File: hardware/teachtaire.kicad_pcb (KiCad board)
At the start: 4 copper layers, 60 x 60 mm, 50 parts, among them J1 Conn_Coaxial, J3 ESQ-110-X-X-D, J4 XT30PW-M, J5 Conn_01x10, J6 Conn_Coaxial, Q1 PMOS, Q2 NMOS, U1 MAX-M10S, U10 radio_thing, U2 STM32F072C8Tx, U3 TJA1051T/3/1J, U4 TLV70433DBVT, U5 LT6003HDC-TRMPBF, U6 NC7WZ07P6X, U7 NC7WZ07P6X

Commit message: minorest of changes
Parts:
- removed U10: radio_thing, radio_breakout:radio_breakout
- added G***: LOGO, LOGO, F.Cu at (180.0, 98.5)
- added G***: LOGO, LOGO, F.Cu at (171.0, 111.5)
- added G***: LOGO, LOGO, F.Cu at (154.0, 81.0)
- added U8: RF-LORA-868-SO, footprints:XCVR_RF-LORA-868-SO, F.Cu at (146.0, 95.2)
- moved U5 22.9 mm to (179.4, 88.1), turned to 0 degrees
- moved J6 19.9 mm to (153.6, 73.3)
- moved D1 16.9 mm to (165.7, 101.0), turned to 180 degrees
- moved C28 15.8 mm to (167.6, 113.9), turned to -90 degrees
- moved R1 15.2 mm to (163.8, 101.0), turned to 0 degrees
- moved C30 14.3 mm to (166.6, 113.9), turned to -90 degrees
- moved C31 13.8 mm to (155.2, 112.7), turned to 180 degrees
- moved C2 12.0 mm to (176.0, 91.4)
- moved R3 11.1 mm to (171.6, 88.7), turned to -90 degrees
- moved Q2 10.4 mm to (172.2, 92.5)
- moved J1 10.2 mm to (175.5, 96.7), turned to 180 degrees
- moved Q1 9.99 mm to (174.1, 89.2)
- moved C39 9.76 mm to (163.7, 86.3), turned to 0 degrees
- moved C1 9.40 mm to (175.0, 93.6), turned to 180 degrees
- moved U4 9.24 mm to (160.5, 86.0), turned to 180 degrees
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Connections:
- Q1 pad 1: +3.3V -> /GNSS_Bias_T/Antenna Supply
- R3 pad 1: +3.3V -> /GNSS_Bias_T/Antenna Supply
- U1 pad 14: unconnected-(U1-VCC_RF-Pad14) -> /GNSS_Bias_T/Antenna Supply
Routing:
- net GND: track 89.7 -> 8.82 mm, vias 34 -> 120
- net 5VLOGIC: track 62.4 -> 30.7 mm, vias 5 -> 1
- net Net-(J6-In): track 45.4 -> 14.5 mm
- net Net-(U5--IN): track 40.0 -> 12.1 mm, vias 2 -> 0
- net Net-(U5-+IN): track 27.2 -> 3.06 mm, vias 2 -> 0
- net LoRa_NSS: track 36.5 -> 17.4 mm
- net /GNSS_Bias_T/Antenna Supply: track 0.00 -> 16.3 mm, vias 0 -> 2
- net /GNSS_Bias_T/ANT_OFF_N: track 18.9 -> 4.18 mm, vias 2 -> 0
- net LoRa_MOSI: track 33.6 -> 19.1 mm
- net /GNSS_Bias_T/V_ANT: track 21.4 -> 8.03 mm, vias 2 -> 0
- net Net-(J1-In): track 15.8 -> 2.46 mm, vias 2 -> 0
- net SWCLK1: track 56.7 -> 44.5 mm, vias 4 -> 1
- net LoRa_MISO: track 33.4 -> 21.4 mm
- net Net-(Q1-S): track 11.4 -> 2.23 mm
- net Net-(U1-TIMEPULSE): track 2.13 -> 10.1 mm
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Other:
- board text added: "Teachtaire V1.0"

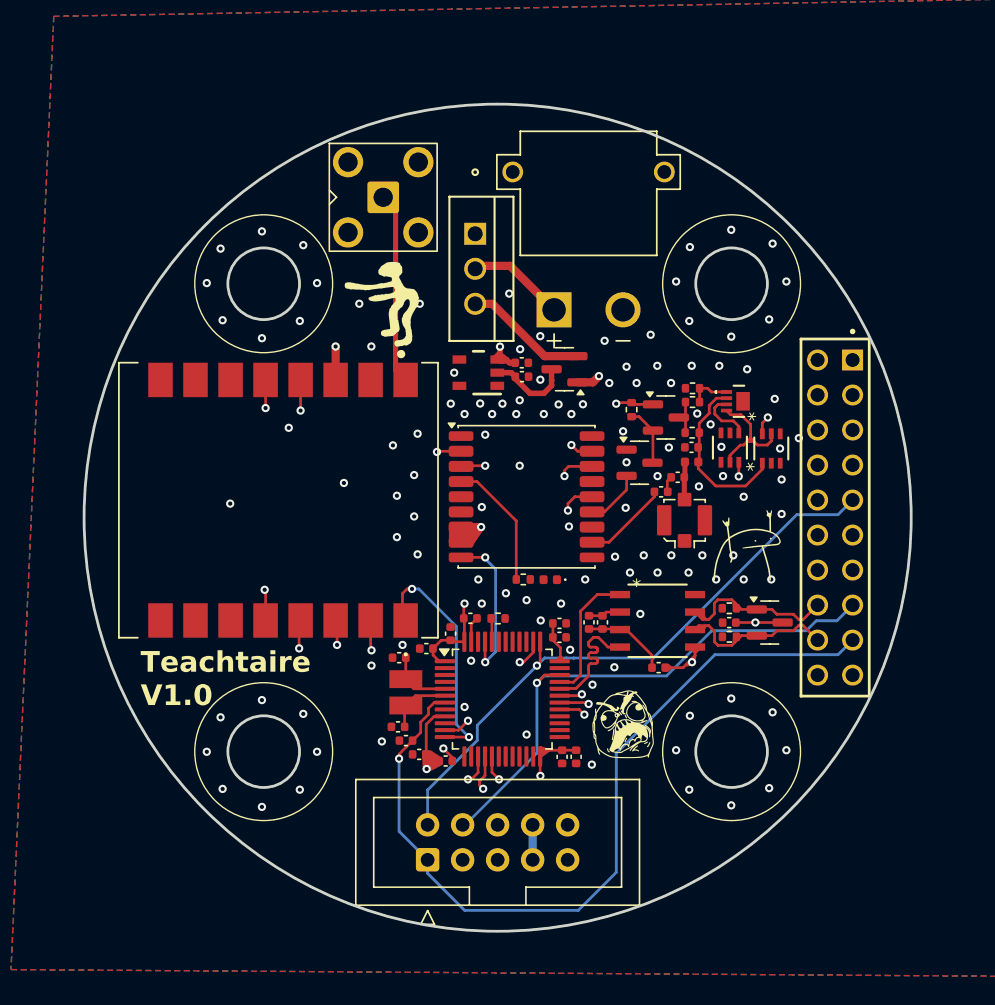
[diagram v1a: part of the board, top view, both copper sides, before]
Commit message: Changes from Reddit review 1
Changed connector, impedance matched the RF traces, changed board to square
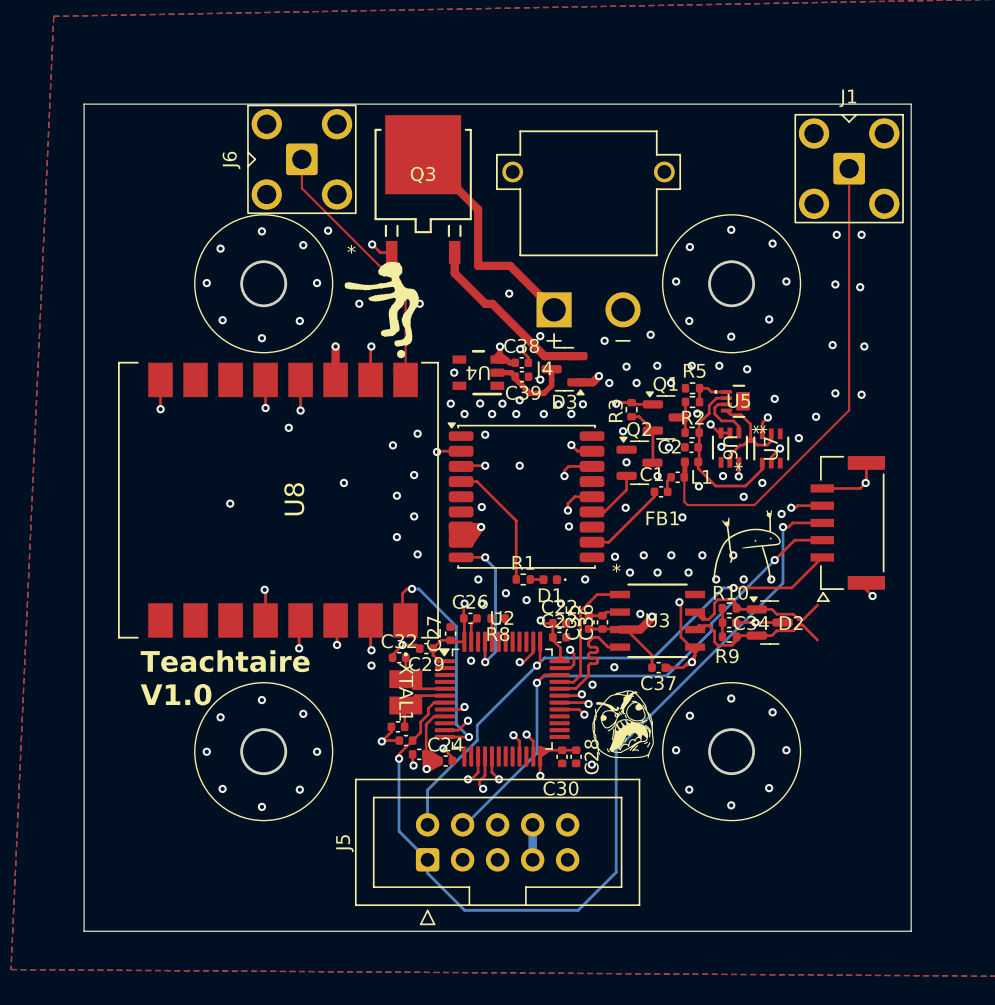
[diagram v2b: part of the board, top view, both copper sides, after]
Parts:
- removed J3: ESQ-110-X-X-D, footprints:SAMTEC_ESQ-110-14-G-D
- removed MOSFET1: IPP80P03P4L04AKSA1, footprints:IPP80P03P4L04AKSA1
- added J2: 5023860570, footprints:MOLEX_5023860570, F.Cu at (187.4, 96.9)
- added Q3: IPD90P04P4L04ATMA1, footprints:PG-TO252-3-313_INF-L, F.Cu at (156.5, 71.6)
- J1: footprint Connector_Coaxial:U.FL_Molex_MCRF_73412-0110_Vertical -> Connector_Coaxial:SMA_BAT_Wireless_BWSMA-KWE-Z001
- moved J1 28.2 mm to (187.4, 71.2), turned to -90 degrees
- moved J6 6.51 mm to (147.7, 70.5)
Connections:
- U2 pad 21: unconnected-(U2-PB10-Pad21) -> LoRa_DIO2
- U8 pad 8: unconnected-(U8-DIO2-Pad8) -> LoRa_DIO2
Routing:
- net LoRa_DIO2: track 0.00 -> 39.6 mm, vias 0 -> 2
- net Net-(J1-In): track 2.46 -> 35.2 mm
- net GND: track 8.82 -> 34.8 mm, vias 120 -> 135
- net 5VLOGIC: track 30.7 -> 55.1 mm, vias 1 -> 2
- net +3.3V: track 128.3 -> 147.2 mm, vias 8 -> 10
- net Net-(Q3-D): track 7.13 -> 16.5 mm
- net Net-(J6-In): track 14.5 -> 20.7 mm
- net SWCLK1: track 44.5 -> 40.6 mm, vias 1 -> 2
- net Net-(Q3-S): track 8.99 -> 12.9 mm
- net NRST: track 60.2 -> 64.0 mm, vias 1 -> 2
- net 5VSERVO: track 2.54 -> 0.00 mm
- net Net-(C34-Pad1): track 0.00 -> 2.08 mm
- net Net-(D1-A): track 0.00 -> 0.97 mm
- net SWDIO: vias 1 -> 2
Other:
- outline, holes or cut-outs redrawn

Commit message: lots to be sorted
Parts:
- removed J5: Conn_01x10, Connector_IDC:IDC-Header_2x05_P2.54mm_Vertical
- added G***: LOGO, LOGO, F.Cu at (140.3, 122.8)
- added J3: ESQ-110-X-X-D, footprints:SAMTEC_ESQ-110-14-G-D, F.Cu at (187.6, 96.3)
- moved J2 35.5 mm to (162.2, 122.0), turned to 180 degrees
- moved G*** 2.00 mm to (156.0, 81.0)
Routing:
- added copper zone on In3.Cu, net GND
- added copper zone on In4.Cu, net GND
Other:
- copper layers 4 -> 6
- board text added: "SWCLK SWDIO NRST 3v3 GND"
- board text added: "teachtaire-v1.0"
- board text removed: "Teachtaire V1.0"

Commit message: many fatal fuck-ups found
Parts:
- removed C38: 1uF, Capacitor_SMD:C_0402_1005Metric
- removed C39: 100nF, Capacitor_SMD:C_0402_1005Metric
- removed FB1: FerriteBead, Capacitor_SMD:C_0402_1005Metric
- added C10: 0.1uf, Capacitor_SMD:C_0402_1005Metric, F.Cu at (208.2, 116.1)
- added C11: 4.7uF, Capacitor_SMD:C_0402_1005Metric, F.Cu at (97.9, 71.0)
- added C12: 100nF, Capacitor_SMD:C_0402_1005Metric, F.Cu at (97.9, 72.9)
- added C13: 4.7uF, Capacitor_SMD:C_0402_1005Metric, F.Cu at (97.9, 74.9)
- added C14: 100nF, Capacitor_SMD:C_0402_1005Metric, F.Cu at (97.9, 76.9)
- added C3: 39pf, Capacitor_SMD:C_0402_1005Metric, F.Cu at (205.4, 110.2)
- added C4: 0.1uf, Capacitor_SMD:C_0402_1005Metric, F.Cu at (205.4, 112.2)
- added C47: 22uf, Capacitor_SMD:C_0402_1005Metric, F.Cu at (211.1, 110.2)
- added C48: 22uf, Capacitor_SMD:C_0402_1005Metric, F.Cu at (211.1, 112.2)
- added C5: 22uf, Capacitor_SMD:C_0402_1005Metric, F.Cu at (205.4, 114.2)
- added C50: 1uf, Capacitor_SMD:C_0402_1005Metric, F.Cu at (211.1, 114.2)
- added C51: 1uf, Capacitor_SMD:C_0402_1005Metric, F.Cu at (211.1, 116.1)
- added C6: 22uf, Capacitor_SMD:C_0402_1005Metric, F.Cu at (205.4, 116.1)
- added C7: 1uf, Capacitor_SMD:C_0402_1005Metric, F.Cu at (208.2, 110.2)
- added C8: 22uf, Capacitor_SMD:C_0402_1005Metric, F.Cu at (208.2, 112.2)
- added C9: 22uf, Capacitor_SMD:C_0402_1005Metric, F.Cu at (208.2, 114.2)
- added GND1: TestPoint, TestPoint:TestPoint_Pad_D2.0mm, F.Cu at (94.5, 72.0)
- added Q4: NMOS, Package_TO_SOT_SMD:SOT-23, F.Cu at (101.8, 72.2)
- added R11: 10kΩ, Resistor_SMD:R_0402_1005Metric, F.Cu at (100.8, 75.4)
- added R12: 100kΩ, Resistor_SMD:R_0402_1005Metric, F.Cu at (214.0, 114.2)
- added R14: 0Ω, Resistor_SMD:R_0402_1005Metric, F.Cu at (93.9, 81.1)
- added R15: 0Ω, Resistor_SMD:R_0402_1005Metric, F.Cu at (93.9, 83.1)
- added R6: 10kΩ, Resistor_SMD:R_0402_1005Metric, F.Cu at (214.0, 110.2)
- added R7: 53.6kΩ, Resistor_SMD:R_0402_1005Metric, F.Cu at (214.0, 112.2)
- added U9: TLV75533PDRV, Package_SON:WSON-6-1EP_2x2mm_P0.65mm_EP1x1.6mm, F.Cu at (205.8, 119.0)
- added VBCKP1: TestPoint, TestPoint:TestPoint_Pad_D2.0mm, F.Cu at (94.5, 76.1)
- J4: value XT30PW-M -> 39-29-1048; footprint footprints:AMASS_XT30PW-M -> footprints:MOLEX_39-29-1048
- R10, R9: value 60 Ω -> 60Ω
- U4: value TLV70433DBVT -> MPM3650CGQW-P; footprint footprints:DBV0005A_N -> footprints:QFN-24_MPM3650_MNP
- moved J1 101.7 mm to (87.5, 52.0), turned to 0 degrees
- moved D1 99.6 mm to (71.2, 69.4), turned to 0 degrees
- moved R1 95.9 mm to (73.2, 69.5), turned to 180 degrees
- moved L1 95.4 mm to (87.1, 57.9), turned to 180 degrees
- moved U1 94.6 mm to (75.0, 63.0), turned to 90 degrees
- moved C1 94.4 mm to (88.0, 56.8), turned to 0 degrees
- moved Q1 80.3 mm to (98.9, 61.3)
- moved Q2 80.3 mm to (96.9, 64.6)
- moved R2 80.3 mm to (100.8, 62.4)
- moved R3 80.3 mm to (96.4, 60.7)
- moved R4 80.3 mm to (100.8, 60.2)
- moved R5 80.3 mm to (100.8, 59.2)
- moved U5 80.3 mm to (104.2, 60.1)
- moved C2 80.3 mm to (100.7, 63.5)
- moved U6 80.3 mm to (103.5, 63.5)
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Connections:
- net SWCLK1 renamed SWCLK
- C1 pad 2: Net-(C1-Pad2) -> /GNSS_Bias_T/RF_IN
- C22 pad 1: +3.3V -> +3V3D
- C23 pad 1: +3.3V -> +3V3D
- C24 pad 1: +3.3V -> +3V3D
- C25 pad 1: +3.3V -> +3V3D
- C26 pad 1: +3.3V -> +3V3D
- C27 pad 1: +3.3V -> +3V3D
- C28 pad 1: +3.3V -> +3V3D
- C29 pad 1: +3.3V -> +3V3D
- C30 pad 1: +3.3V -> +3V3D
- C37 pad 1: +3.3V -> 5VLOGIC
- C37 pad 2: 5VLOGIC -> +3V3D
- D1 pad 1: GND -> Net-(D1-K)
- Q1 pad 1: /GNSS_Bias_T/Antenna Supply -> Net-(Q1-D)
- Q1 pad 3: Net-(Q1-S) -> /GNSS_Bias_T/Antenna Supply
- Q2 pad 1: GND -> Net-(Q1-G)
- Q2 pad 3: Net-(Q1-G) -> GND
- R1 pad 1: Net-(U1-TIMEPULSE) -> +3.3V
- R2 pad 2: Net-(Q1-S) -> Net-(Q1-D)
- R4 pad 1: Net-(Q1-S) -> Net-(Q1-D)
- U1 pad 4: Net-(U1-TIMEPULSE) -> Net-(Q4-G)
- U1 pad 6: unconnected-(U1-V_BCKP-Pad6) -> Net-(U1-V_BCKP)
- U1 pad 7: +3.3V -> +3V3RF
- U1 pad 8: +3.3V -> +3V3RF
- U2 pad 1: +3.3V -> +3V3D
- U2 pad 24: +3.3V -> +3V3D
- U2 pad 36: +3.3V -> +3V3D
- U2 pad 48: +3.3V -> +3V3D
- U2 pad 9: +3.3V -> +3V3D
- U3 pad 5: +3.3V -> +3V3D
- U4 pad 2: VBAT -> GND
- U4 pad 3: +3.3V -> GND
- U5 pad 4: /GNSS_Bias_T/V_ANT -> +3V3D
- U6 pad 5: /GNSS_Bias_T/V_ANT -> +3V3D
- U6 pad 6: /GNSS_Bias_T/ANT_DETECT -> Net-(U6-Y1)
- U7 pad 5: /GNSS_Bias_T/V_ANT -> +3V3D
- U7 pad 6: /GNSS_Bias_T/ANT_SHORT_N -> Net-(U7-Y1)
- U8 pad 3: +3.3V -> +3V3RF
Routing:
- net NRST: track 64.0 -> 4.18 mm, vias 2 -> 0
- net +3.3V: track 147.2 -> 97.6 mm, vias 10 -> 0
- net 5VLOGIC: track 55.1 -> 9.41 mm, vias 2 -> 1
- net SWCLK: track 40.6 -> 0.00 mm, vias 2 -> 0
- net SWDIO: track 39.8 -> 0.00 mm, vias 2 -> 0
- net LoRa_DIO2: track 39.6 -> 1.72 mm, vias 2 -> 1
- net LoRa_RX_SWITCH: track 35.4 -> 1.95 mm, vias 2 -> 1
- net Net-(J1-In): track 35.2 -> 5.97 mm
- net LoRa_TX_SWITCH: track 30.6 -> 1.60 mm, vias 2 -> 1
- net LoRa_RESET: track 25.1 -> 1.96 mm, vias 2 -> 1
- net PA10: track 25.9 -> 3.20 mm
- net PA9: track 25.1 -> 3.69 mm
- net Net-(J6-In): track 20.7 -> 0.00 mm
- net LoRa_SCK: track 22.0 -> 1.42 mm, vias 2 -> 1
- net +3V3D: track 0.00 -> 20.5 mm, vias 0 -> 4
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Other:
- outline, holes or cut-outs redrawn
- board text added: "backup pwr"
- board text added: "teachtaire-v1.2"
- board text removed: "teachtaire-v1.0"

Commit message: fixed the fuck-ups
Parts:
- removed the C10 at (208.2, 116.1)
- removed the C3 at (205.4, 110.2)
- removed the C4 at (205.4, 112.2)
- removed the C5 at (205.4, 114.2)
- removed the C6 at (205.4, 116.1)
- removed the C7 at (208.2, 110.2)
- removed the C8 at (208.2, 112.2)
- removed the C9 at (208.2, 114.2)
- removed the R6 at (214.0, 110.2)
- removed the R7 at (214.0, 112.2)
- removed the U4 at (213.0, 121.1)
- added C23: 39pf, Capacitor_SMD:C_0402_1005Metric, F.Cu at (188.9, 70.8)
- added C24: 0.1uf, Capacitor_SMD:C_0402_1005Metric, F.Cu at (188.9, 72.8)
- added C25: 22uf, Capacitor_SMD:C_0402_1005Metric, F.Cu at (188.9, 74.7)
- added C26: 22uf, Capacitor_SMD:C_0402_1005Metric, F.Cu at (188.9, 76.7)
- added C28: 1uf, Capacitor_SMD:C_0402_1005Metric, F.Cu at (188.9, 78.7)
- added C30: 22uf, Capacitor_SMD:C_0402_1005Metric, F.Cu at (188.9, 80.7)
- added C31: 22uf, Capacitor_SMD:C_0402_1005Metric, F.Cu at (191.8, 70.8)
- added C32: 0.1uf, Capacitor_SMD:C_0402_1005Metric, F.Cu at (191.8, 72.8)
- added C34: 4.7uf, Capacitor_SMD:C_0402_1005Metric, F.Cu at (191.8, 74.7)
- added C35: 4.7uf, Capacitor_SMD:C_0402_1005Metric, F.Cu at (191.8, 76.7)
- added C37: 10uf, Capacitor_SMD:C_0402_1005Metric, F.Cu at (191.8, 78.7)
- added D4: BAT54J, Diode_SMD:D_SOD-323F, F.Cu at (135.7, 117.5)
- added R13: 53.6kΩ, Resistor_SMD:R_0402_1005Metric, F.Cu at (201.0, 72.8)
- added R14: 100kΩ, Resistor_SMD:R_0402_1005Metric, F.Cu at (201.0, 74.8)
- added R15: 33.2kΩ, Resistor_SMD:R_0402_1005Metric, F.Cu at (201.0, 76.8)
- added U8: MPM3650CGQW-P, footprints:QFN-24_MPM3650_MNP, F.Cu at (190.2, 86.3)
- added VR1: LT3045EDD_PBF, footprints:SON50P300X300X80-11N, F.Cu at (202.2, 85.6)
- R12: value 100kΩ -> 10kΩ
- moved J5 100.2 mm to (161.3, 119.8), turned to -90 degrees
- moved L1 91.7 mm to (155.1, 119.3), turned to 90 degrees
- moved C21 90.1 mm to (152.4, 119.8), turned to 180 degrees
- moved U1 88.5 mm to (145.5, 116.5), turned to 0 degrees
- moved R8 80.8 mm to (161.0, 114.0)
- moved R9 80.8 mm to (161.0, 113.0)
- moved U6 80.6 mm to (166.7, 113.4), turned to 90 degrees
- moved U5 79.6 mm to (163.5, 113.1), turned to 90 degrees
- moved R7 79.0 mm to (152.1, 116.7)
- moved Q4 78.2 mm to (157.9, 113.5)
- moved D1 77.9 mm to (134.7, 114.5), turned to 180 degrees
- moved R6 77.5 mm to (156.5, 116.3), turned to 90 degrees
- moved C22 77.2 mm to (155.6, 117.8), turned to 0 degrees
- moved Q3 76.7 mm to (153.6, 115.1), turned to 180 degrees
- moved R2 74.7 mm to (132.8, 114.5), turned to 0 degrees
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- renumbered C11 to C1, C26 to C10, C24 to C11, C25 to C12, C22 to C13, C23 to C14, C35 to C15, C36 to C16, C37 to C17, C13 to C18, C14 to C19, C12 to C2, C34 to C20, C1 to C21, C2 to C22, C48 to C27, C47 to C29, C29 to C3, C50 to C33, C51 to C36, C30 to C4, C32 to C5, C33 to C6, C31 to C7, C28 to C8, C27 to C9, D3 to D2, D2 to D3, J4 to J1, J3 to J2, J6 to J3, J2 to J4, J1 to J5, Q4 to Q1, Q3 to Q2, Q1 to Q3, Q2 to Q4, R11 to R1, R14 to R10, R15 to R11, R1 to R2, R8 to R3, R10 to R4, R9 to R5, R2 to R6, R3 to R7, R4 to R8, R5 to R9, U8 to U4
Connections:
- C36 pad 1: +3V3RF -> +3V3D
- R12 pad 1: Net-(R12-Pad1) -> GND
- U1 pad 6: Net-(U1-V_BCKP) -> Net-(D4-K)
- U9 pad 1: +3V3RF -> +3V3D
- VBCKP1 pad 1: Net-(U1-V_BCKP) -> Net-(D4-A)
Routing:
- net +3.3V: track 97.6 -> 0.96 mm, vias 0 -> 1
- net Net-(U5--IN): track 0.00 -> 20.6 mm, vias 0 -> 2
- net VBAT: track 0.00 -> 19.8 mm, vias 0 -> 4
- net /GNSS_Bias_T/ANT_OFF_N: track 0.00 -> 13.3 mm, vias 0 -> 2
- net CAN_-: track 3.91 -> 16.6 mm
- net Net-(U6-Y1): track 0.00 -> 12.4 mm
- net CAN_+: track 4.38 -> 16.5 mm
- net Net-(U8-VCC): track 0.00 -> 10.8 mm, vias 0 -> 2
- net /GNSS_Bias_T/Antenna Supply: track 11.9 -> 3.33 mm
- net Net-(Q3-G): track 0.00 -> 7.13 mm
- net GND: track 17.8 -> 24.7 mm, vias 45 -> 124
- net Net-(Q3-D): track 0.00 -> 6.78 mm
- net Net-(U9-EN): track 0.00 -> 6.50 mm
- net Net-(J3-In): track 0.00 -> 6.30 mm
- net +3V3D: track 20.5 -> 25.8 mm, vias 4 -> 7
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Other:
- board text removed: "backup pwr"
